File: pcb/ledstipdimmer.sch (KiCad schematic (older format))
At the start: 42 parts, among them P1 SolderCable, P2 SolderCable, Q1 NTTFS5820NLTAG, Q2 NTTFS5820NLTAG, T1 TOUCH, U1 TPS7B6950, U2 IQS904D

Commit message: PCB design waiting for review.
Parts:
- added C10, C11, C8, C9: 10n, kicap_rescap:SMD-C-0603, symbol C_Small
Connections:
- net +24V: now also P2.2 (P2); no longer P2.1 (P1)
- net BL: now also C10.2, C11.2, C8.2, C9.2
- net LD1: now also C8.1
- net LD2: now also C9.1
- net LD3: now also C10.1
- net LD4: now also C11.1
- net LOAD: now also P2.1 (P1); no longer P2.2 (P2)
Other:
- note added: "Touch Area\nKeep Clearance"
- note removed: "Touch Area\nGuard with GND"
- moved on the sheet: D1, D2, D3, D4, R3, R4, R5, R6, W10, W3, W5, W7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

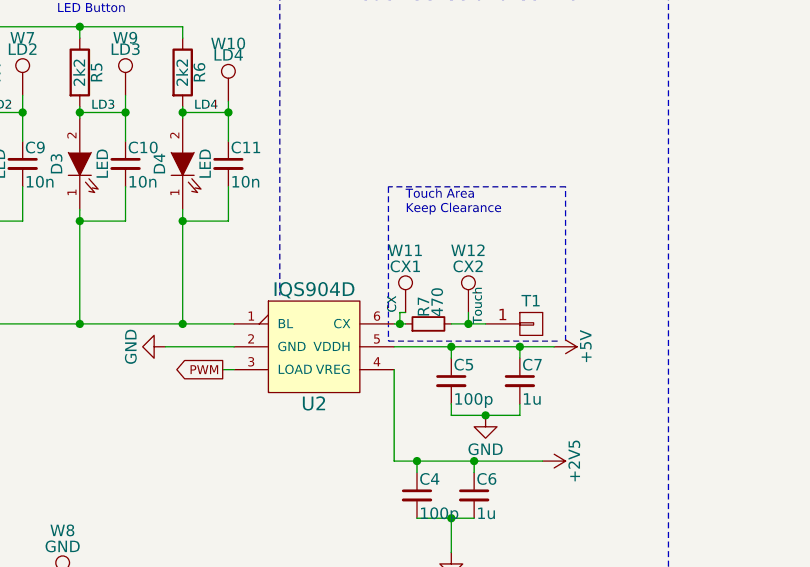
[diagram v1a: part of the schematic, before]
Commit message: Resolved DRC conflicts. Adjustments left.
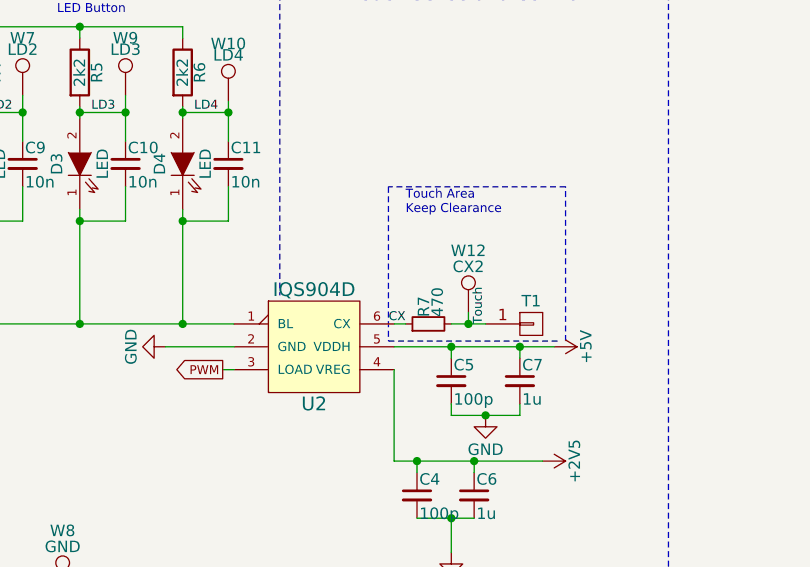
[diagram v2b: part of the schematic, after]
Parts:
- removed W11: CX1, pogo:RECP_709150001050006, symbol TEST_1P
- D5: footprint Diodes_SMD:SMA_Standard -> Diodes_SMD:SMA_Bipolar
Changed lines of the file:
@@
 $EndComp
 $Comp
-L +24V #PWR2
+L +24V #PWR01
 U 1 1 585E6502
 P 1250 1350
-F 0 "#PWR2" H 1250 1200 50  0001 C CNN
+F 0 "#PWR01" H 1250 1200 50  0001 C CNN
 F 1 "+24V" H 1250 1490 50  0000 C CNN
 F 2 "" H 1250 1350 50  0000 C CNN
@@
 $EndComp
 $Comp
-L +5V #PWR6
+L +5V #PWR02
 U 1 1 585E6706
 P 4600 1750
-F 0 "#PWR6" H 4600 1600 50  0001 C CNN
+F 0 "#PWR02" H 4600 1600 50  0001 C CNN
 F 1 "+5V" H 4600 1890 50  0000 C CNN
 F 2 "" H 4600 1750 50  0000 C CNN
@@
 $EndComp
 $Comp
-L +2V5 #PWR15
+L +2V5 #PWR03
 U 1 1 585E6750
 P 8250 2600
-F 0 "#PWR15" H 8250 2450 50  0001 C CNN
+F 0 "#PWR03" H 8250 2450 50  0001 C CNN
 F 1 "+2V5" H 8250 2740 50  0000 C CNN
 F 2 "" H 8250 2600 50  0000 C CNN
@@
 $EndComp
 $Comp
-L +24V #PWR17
+L +24V #PWR04
 U 1 1 585E6A51
 P 10250 900
-F 0 "#PWR17" H 10250 750 50  0001 C CNN
+F 0 "#PWR04" H 10250 750 50  0001 C CNN
 F 1 "+24V" H 10250 1040 50  0000 C CNN
 F 2 "" H 10250 900 50  0000 C CNN
@@
 	9750 1300 10350 1300
 $Comp
-L GND #PWR18
+L GND #PWR05
 U 1 1 585E6CB8
 P 10250 1900
-F 0 "#PWR18" H 10250 1650 50  0001 C CNN
+F 0 "#PWR05" H 10250 1650 50  0001 C CNN
 F 1 "GND" H 10250 1750 50  0000 C CNN
 F 2 "" H 10250 1900 50  0000 C CNN
@@
 F 0 "D5" H 1550 2000 50  0000 C CNN
 F 1 "SMAJ28CA" H 1550 1700 50  0000 C CNN
-F 2 "Diodes_SMD:SMA_Standard" H 1550 1850 50  0001 C CNN
+F 2 "Diodes_SMD:SMA_Bipolar" H 1550 1850 50  0001 C CNN
 F 3 "http://www.mouser.com/ds/2/389/smaj-955168.pdf" H 1550 1850 50  0001 C CNN
 	1    1550 1850
@@
 	1150 2750 1150 3000
 $Comp
-L GND #PWR1
+L GND #PWR06
 U 1 1 585E7C2D
 P 1150 3000
-F 0 "#PWR1" H 1150 2750 50  0001 C CNN
+F 0 "#PWR06" H 1150 2750 50  0001 C CNN
 F 1 "GND" H 1150 2850 50  0000 C CNN
 F 2 "" H 1150 3000 50  0000 C CNN
@@
 Connection ~ 1150 2900
 $Comp
-L +5V #PWR3
+L +5V #PWR07
 U 1 1 585E7EDD
 P 1650 2500
-F 0 "#PWR3" H 1650 2350 50  0001 C CNN
+F 0 "#PWR07" H 1650 2350 50  0001 C CNN
 F 1 "+5V" H 1650 2640 50  0000 C CNN
 F 2 "" H 1650 2500 50  0000 C CNN
@@
 Connection ~ 1650 2900
 $Comp
-L GND #PWR7
+L GND #PWR08
 U 1 1 585E870D
 P 4600 2400
-F 0 "#PWR7" H 4600 2150 50  0001 C CNN
+F 0 "#PWR08" H 4600 2150 50  0001 C CNN
 F 1 "GND" H 4600 2250 50  0000 C CNN
 F 2 "" H 4600 2400 50  0000 C CNN
@@
 	1150 1500 2000 1500
 $Comp
-L GND #PWR5
+L GND #PWR09
 U 1 1 585E8FA3
 P 3200 2350
-F 0 "#PWR5" H 3200 2100 50  0001 C CNN
+F 0 "#PWR09" H 3200 2100 50  0001 C CNN
 F 1 "GND" H 3200 2200 50  0000 C CNN
 F 2 "" H 3200 2350 50  0000 C CNN
@@
 Connection ~ 3200 2300
 $Comp
-L +24V #PWR4
+L +24V #PWR010
 U 1 1 585E949E
 P 2700 1650
-F 0 "#PWR4" H 2700 1500 50  0001 C CNN
+F 0 "#PWR010" H 2700 1500 50  0001 C CNN
 F 1 "+24V" H 2700 1790 50  0000 C CNN
 F 2 "" H 2700 1650 50  0000 C CNN
@@
 	7700 2850 7950 2850
 $Comp
-L GND #PWR13
+L GND #PWR011
 U 1 1 585EAAFE
 P 7850 3000
-F 0 "#PWR13" H 7850 2750 50  0001 C CNN
+F 0 "#PWR011" H 7850 2750 50  0001 C CNN
 F 1 "GND" H 7850 2850 50  0000 C CNN
 F 2 "" H 7850 3000 50  0000 C CNN
@@
 $EndComp
 $Comp
-L GND #PWR14
+L GND #PWR012
 U 1 1 585EAEDD
 P 8000 2400
-F 0 "#PWR14" H 8000 2150 50  0001 C CNN
+F 0 "#PWR012" H 8000 2150 50  0001 C CNN
 F 1 "GND" H 8000 2250 50  0000 C CNN
 F 2 "" H 8000 2400 50  0000 C CNN
@@
 PWM
 $Comp
-L GND #PWR12
+L GND #PWR013
 U 1 1 585EB6CF
 P 6600 2100
-F 0 "#PWR12" H 6600 1850 50  0001 C CNN
+F 0 "#PWR013" H 6600 1850 50  0001 C CNN
 F 1 "GND" H 6600 1950 50  0000 C CNN
 F 2 "" H 6600 2100 50  0000 C CNN
@@
 $EndComp
 $Comp
-L +5V #PWR8
+L +5V #PWR014
 U 1 1 5865BDB4
 P 5300 650
-F 0 "#PWR8" H 5300 500 50  0001 C CNN
+F 0 "#PWR014" H 5300 500 50  0001 C CNN
 F 1 "+5V" H 5300 790 50  0000 C CNN
 F 2 "" H 5300 650 50  0000 C CNN
@@
 LED Button
 $Comp
-L +5V #PWR16
+L +5V #PWR015
 U 1 1 585E67C2
 P 8300 2100
-F 0 "#PWR16" H 8300 1950 50  0001 C CNN
+F 0 "#PWR015" H 8300 1950 50  0001 C CNN
 F 1 "+5V" H 8300 2240 50  0000 C CNN
 F 2 "" H 8300 2100 50  0000 C CNN
@@
 $EndComp
 $Comp
-L GND #PWR11
+L GND #PWR016
 U 1 1 58666E88
 P 6150 3225
-F 0 "#PWR11" H 6150 2975 50  0001 C CNN
+F 0 "#PWR016" H 6150 2975 50  0001 C CNN
 F 1 "GND" H 6150 3075 50  0000 C CNN
 F 2 "" H 6150 3225 50  0000 C CNN
@@
 $EndComp
 $Comp
-L +2V5 #PWR10
+L +2V5 #PWR017
 U 1 1 58666FD2
 P 5800 3275
-F 0 "#PWR10" H 5800 3125 50  0001 C CNN
+F 0 "#PWR017" H 5800 3125 50  0001 C CNN
 F 1 "+2V5" H 5800 3415 50  0000 C CNN
 F 2 "" H 5800 3275 50  0000 C CNN
@@
 $EndComp
 $Comp
-L +5V #PWR9
+L +5V #PWR018
 U 1 1 586670E2
 P 5450 3275
-F 0 "#PWR9" H 5450 3125 50  0001 C CNN
+F 0 "#PWR018" H 5450 3125 50  0001 C CNN
 F 1 "+5V" H 5450 3415 50  0000 C CNN
 F 2 "" H 5450 3275 50  0000 C CNN
@@
 	9125 3475 9250 3475
 $Comp
-L TEST_1P W11
-U 1 1 58669762
-P 7650 1950
-F 0 "W11" H 7650 2220 50  0000 C CNN
-F 1 "CX1" H 7650 2150 50  0000 C CNN
-F 2 "pogo:RECP_709150001050006" H 7850 1950 50  0001 C CNN
-F 3 "" H 7850 1950 50  0000 C CNN
-	1    7650 1950
-	1    0    0    -1
-$EndComp
-$Comp
 L TEST_1P W12
 U 1 1 58669C58
@@
 	7925 1950 7925 2000
 Connection ~ 7925 2000
-Wire Wire Line
-	7650 1950 7625 1950
-Wire Wire Line
-	7625 1950 7625 2000
-Connection ~ 7625 2000
 Wire Notes Line
 	8350 2075 8350 1400
@@
 Text Label 8000 2000 1    39   ~ 0
 Touch
-Text Label 7625 1950 1    39   ~ 0
-CX
 Text Label 5400 2000 0    39   ~ 0
 BL
@@
 Text Notes 7650 1525 0    39   ~ 0
 Touch Area\nKeep Clearance
+Text Label 7650 2000 2    39   ~ 0
+CX
 $EndSCHEMATC

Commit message: Uploaded script.
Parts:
- removed D5: SMAJ28CA, Diodes_SMD:SMA_Bipolar, symbol TVS
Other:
- moved on the sheet: W1
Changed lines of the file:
@@
 EESchema Schematic File Version 2
-LIBS:texas
 LIBS:linear
-LIBS:tps7b6950
-LIBS:regul
-LIBS:azoteq
 LIBS:transistors
 LIBS:device
 LIBS:conn
 LIBS:power
-LIBS:diode
 LIBS:ledstipdimmer-cache
 EELAYER 25 0
@@
 	9750 1600 9950 1600
 $Comp
-L TVS D5
-U 1 1 585E6EB9
-P 1550 1850
-F 0 "D5" H 1550 2000 50  0000 C CNN
-F 1 "SMAJ28CA" H 1550 1700 50  0000 C CNN
-F 2 "Diodes_SMD:SMA_Bipolar" H 1550 1850 50  0001 C CNN
-F 3 "http://www.mouser.com/ds/2/389/smaj-955168.pdf" H 1550 1850 50  0001 C CNN
-	1    1550 1850
-	0    1    1    0
-$EndComp
-$Comp
 L C C1
 U 1 1 585E7186
@@
 Connection ~ 1250 1500
 Wire Wire Line
-	1550 1425 1550 1550
-Wire Wire Line
 	1150 2350 1150 1600
-Wire Wire Line
-	1550 2150 1550 2250
-Wire Wire Line
-	1550 2250 1150 2250
-Connection ~ 1150 2250
 Connection ~ 1550 1500
 Wire Wire Line
@@
 L TEST_1P W1
 U 1 1 58670110
-P 1550 1425
-F 0 "W1" H 1550 1695 50  0000 C CNN
-F 1 "24V" H 1550 1625 50  0000 C CNN
-F 2 "pogo:RECP_709150001050006" H 1750 1425 50  0001 C CNN
-F 3 "" H 1750 1425 50  0000 C CNN
-	1    1550 1425
+P 1550 1350
+F 0 "W1" H 1550 1620 50  0000 C CNN
+F 1 "24V" H 1550 1550 50  0000 C CNN
+F 2 "pogo:RECP_709150001050006" H 1750 1350 50  0001 C CNN
+F 3 "" H 1750 1350 50  0000 C CNN
+	1    1550 1350
 	1    0    0    -1
 $EndComp
@@
 Text Label 3275 1850 0    39   ~ 0
 Vi
-Text Label 1275 2250 0    39   ~ 0
+Text Label 1150 2200 0    39   ~ 0
 PWRm
 $Comp
@@
 Text Label 7650 2000 2    39   ~ 0
 CX
+Wire Wire Line
+	1550 1350 1550 1500
 $EndSCHEMATC
